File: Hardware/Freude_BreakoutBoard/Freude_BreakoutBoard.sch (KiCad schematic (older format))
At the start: 11 parts, among them J10 Conn_01x06_Female, J11 Conn_01x05_Male, J12 Conn_01x05_Female, J5 Conn_01x06_Female, J6 Conn_01x06_Male, J7 Conn_01x03_Female, J8 Conn_01x06_Male, J9 Conn_01x06_Female, U3 TLV713185PDBV

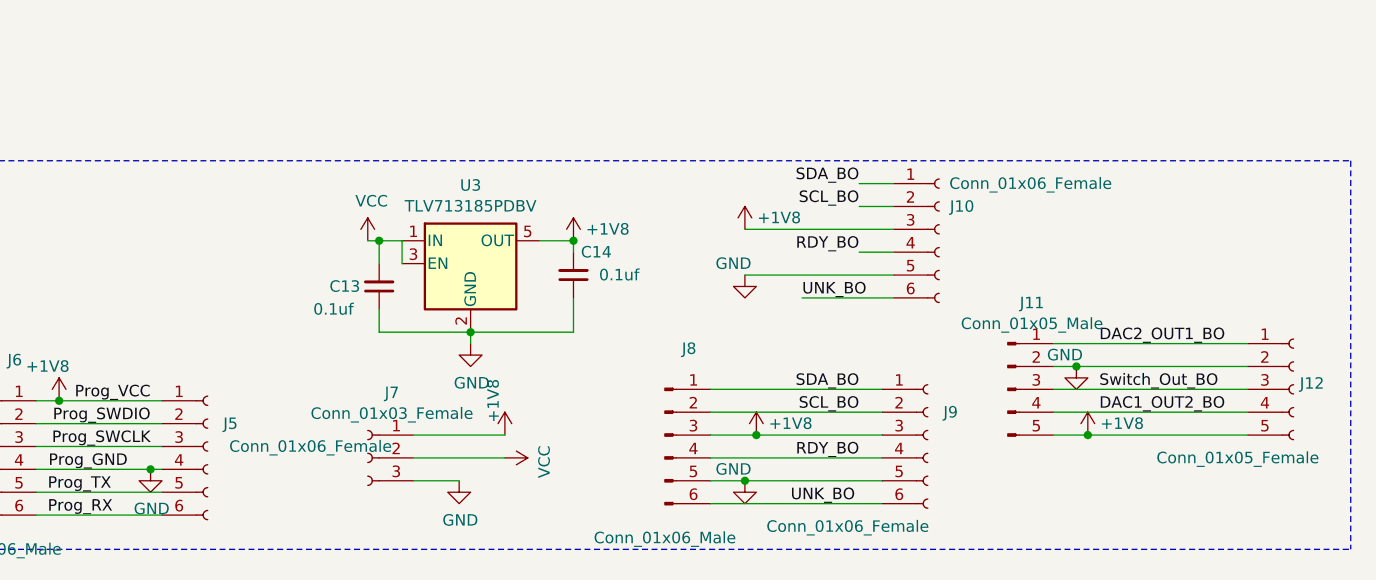
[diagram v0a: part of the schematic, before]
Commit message: resolves 10, resolves 9, resolves 6, resolves 5, add ground ring around touch sensor, add ground ring on top, separate RX from TX and include ground plane between
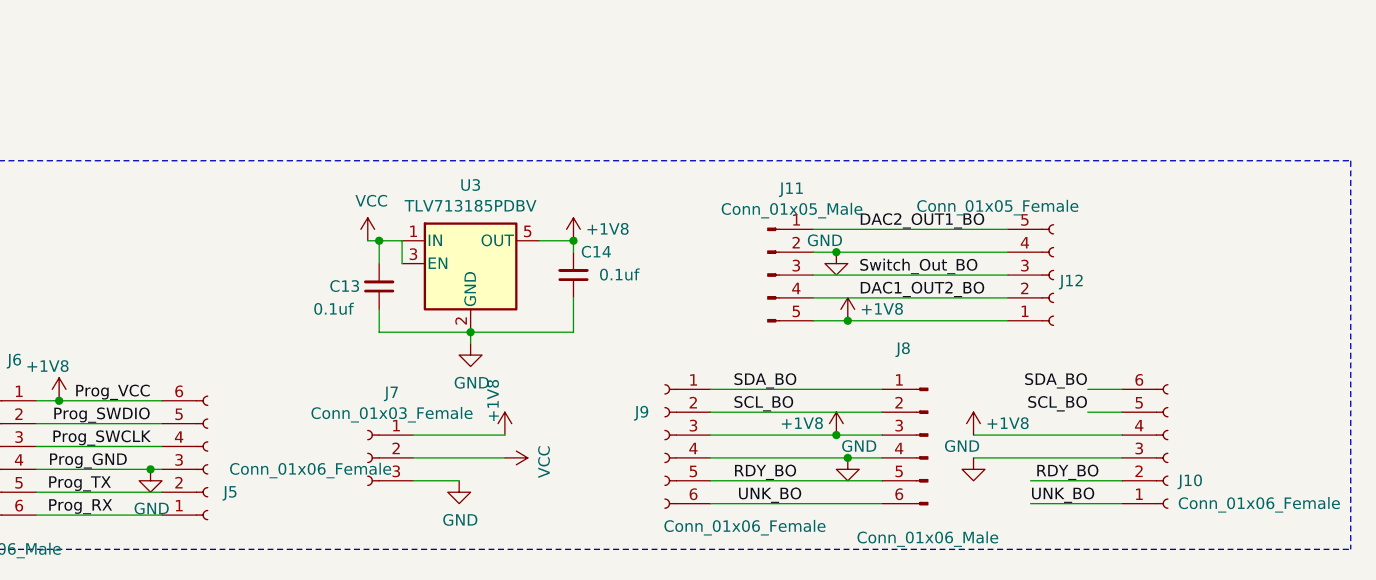
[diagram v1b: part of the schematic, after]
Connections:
- net +1V8: now also J10.4 (Pin_4), J12.1 (Pin_1), J5.6 (Pin_6); no longer J10.3 (Pin_3), J12.5 (Pin_5), J5.1 (Pin_1)
- net DAC1_OUT2_BO: now also J12.2 (Pin_2); no longer J12.4 (Pin_4)
- net DAC2_OUT1_BO: now also J12.5 (Pin_5); no longer J12.1 (Pin_1)
- net GND: now also J10.3 (Pin_3), J12.4 (Pin_4), J5.3 (Pin_3), J8.4 (Pin_4), J9.4 (Pin_4); no longer J10.5 (Pin_5), J12.2 (Pin_2), J5.4 (Pin_4), J8.5 (Pin_5), J9.5 (Pin_5)
- net Prog_RX: now also J5.1 (Pin_1); no longer J5.6 (Pin_6)
- net Prog_SWCLK: now also J5.4 (Pin_4); no longer J5.3 (Pin_3)
- net Prog_SWDIO: now also J5.5 (Pin_5); no longer J5.2 (Pin_2)
- net Prog_TX: now also J5.2 (Pin_2); no longer J5.5 (Pin_5)
- net RDY_BO: now also J10.2 (Pin_2), J8.5 (Pin_5), J9.5 (Pin_5); no longer J10.4 (Pin_4), J8.4 (Pin_4), J9.4 (Pin_4)
- net SCL_BO: now also J10.5 (Pin_5); no longer J10.2 (Pin_2)
- net SDA_BO: now also J10.6 (Pin_6); no longer J10.1 (Pin_1)
- net UNK_BO: now also J10.1 (Pin_1); no longer J10.6 (Pin_6)
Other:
- moved on the sheet: J10, J11, J12, J8, J9
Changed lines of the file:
@@
 L Connector:Conn_01x06_Female J9
 U 1 1 5F2319DF
+P 5950 4250
+F 0 "J9" H 6050 4350 50  0000 C CNN
+F 1 "Conn_01x06_Female" H 5600 3850 50  0000 C CNN
+F 2 ".pretty:503480-0600" H 5950 4250 50  0001 C CNN
+F 3 "~" H 5950 4250 50  0001 C CNN
+	1    5950 4250
+	-1   0    0    -1
+$EndComp
+Text Label 6250 4050 0    50   ~ 0
+SDA_BO
+Text Label 6250 4150 0    50   ~ 0
+SCL_BO
+Text Label 6250 4450 0    50   ~ 0
+RDY_BO
+$Comp
+L Connector:Conn_01x06_Male J8
+U 1 1 5F232158
 P 7100 4250
-F 0 "J9" H 7200 4350 50  0000 C CNN
-F 1 "Conn_01x06_Female" H 6750 3850 50  0000 C CNN
-F 2 ".pretty:503480-0600" H 7100 4250 50  0001 C CNN
+F 0 "J8" H 7206 4628 50  0000 C CNN
+F 1 "Conn_01x06_Male" H 7100 3800 50  0000 C CNN
+F 2 "SparkFun-Connectors:1X06-KIT" H 7100 4250 50  0001 C CNN
 F 3 "~" H 7100 4250 50  0001 C CNN
 	1    7100 4250
-	1    0    0    -1
-$EndComp
-Text Label 6800 4050 2    50   ~ 0
-SDA_BO
-Text Label 6800 4150 2    50   ~ 0
-SCL_BO
-Text Label 6800 4350 2    50   ~ 0
-RDY_BO
-$Comp
-L Connector:Conn_01x06_Male J8
-U 1 1 5F232158
-P 5950 4250
-F 0 "J8" H 6056 4628 50  0000 C CNN
-F 1 "Conn_01x06_Male" H 5950 3800 50  0000 C CNN
-F 2 "SparkFun-Connectors:1X06-KIT" H 5950 4250 50  0001 C CNN
-F 3 "~" H 5950 4250 50  0001 C CNN
-	1    5950 4250
-	1    0    0    -1
-$EndComp
-Wire Wire Line
-	6150 4050 6900 4050
-Wire Wire Line
-	6900 4150 6150 4150
-Wire Wire Line
-	6900 4350 6150 4350
-Wire Wire Line
-	6150 4550 6900 4550
+	-1   0    0    -1
+$EndComp
+Wire Wire Line
+	6900 4050 6150 4050
+Wire Wire Line
+	6150 4150 6900 4150
+Wire Wire Line
+	6900 4550 6150 4550
 $Comp
 L power:+1V8 #PWR0122
 U 1 1 5F274120
-P 6350 4250
-F 0 "#PWR0122" H 6350 4100 50  0001 C CNN
-F 1 "+1V8" H 6500 4300 50  0000 C CNN
-F 2 "" H 6350 4250 50  0001 C CNN
-F 3 "" H 6350 4250 50  0001 C CNN
-	1    6350 4250
-	1    0    0    -1
-$EndComp
-Wire Wire Line
-	6150 4250 6350 4250
-Connection ~ 6350 4250
-Wire Wire Line
-	6350 4250 6900 4250
+P 6700 4250
+F 0 "#PWR0122" H 6700 4100 50  0001 C CNN
+F 1 "+1V8" H 6850 4300 50  0000 C CNN
+F 2 "" H 6700 4250 50  0001 C CNN
+F 3 "" H 6700 4250 50  0001 C CNN
+	1    6700 4250
+	-1   0    0    -1
+$EndComp
+Wire Wire Line
+	6900 4250 6700 4250
+Connection ~ 6700 4250
+Wire Wire Line
+	6700 4250 6150 4250
 $Comp
 L power:+1V8 #PWR0123
@@
 L Connector:Conn_01x05_Female J12
 U 1 1 5F274440
-P 8700 4050
-F 0 "J12" H 8727 4076 50  0000 L CNN
-F 1 "Conn_01x05_Female" H 8100 3750 50  0000 L CNN
-F 2 ".pretty:503480-0500" H 8700 4050 50  0001 C CNN
-F 3 "~" H 8700 4050 50  0001 C CNN
-	1    8700 4050
-	1    0    0    -1
-$EndComp
-Text Label 7850 3850 0    50   ~ 0
+P 7650 3550
+F 0 "J12" H 7677 3576 50  0000 L CNN
+F 1 "Conn_01x05_Female" H 7050 3250 50  0000 L CNN
+F 2 ".pretty:503480-0500" H 7650 3550 50  0001 C CNN
+F 3 "~" H 7650 3550 50  0001 C CNN
+	1    7650 3550
+	1    0    0    1
+$EndComp
+Text Label 6800 3350 0    50   ~ 0
 DAC2_OUT1_BO
-Text Label 7850 4150 0    50   ~ 0
+Text Label 6800 3650 0    50   ~ 0
 DAC1_OUT2_BO
-Text Label 7850 4050 0    50   ~ 0
+Text Label 6800 3550 0    50   ~ 0
 Switch_Out_BO
 $Comp
 L Connector:Conn_01x05_Male J11
 U 1 1 5F28FAAB
-P 7450 4050
-F 0 "J11" H 7556 4428 50  0000 C CNN
-F 1 "Conn_01x05_Male" H 7556 4337 50  0000 C CNN
-F 2 "SparkFun-Connectors:1X05" H 7450 4050 50  0001 C CNN
-F 3 "~" H 7450 4050 50  0001 C CNN
-	1    7450 4050
+P 6400 3550
+F 0 "J11" H 6506 3928 50  0000 C CNN
+F 1 "Conn_01x05_Male" H 6506 3837 50  0000 C CNN
+F 2 "SparkFun-Connectors:1X05" H 6400 3550 50  0001 C CNN
+F 3 "~" H 6400 3550 50  0001 C CNN
+	1    6400 3550
 	1    0    0    -1
 $EndComp
@@
 L power:+1V8 #PWR0124
 U 1 1 5F28FB0B
-P 7800 4250
-F 0 "#PWR0124" H 7800 4100 50  0001 C CNN
-F 1 "+1V8" H 7950 4300 50  0000 C CNN
-F 2 "" H 7800 4250 50  0001 C CNN
-F 3 "" H 7800 4250 50  0001 C CNN
-	1    7800 4250
-	1    0    0    -1
-$EndComp
-Wire Wire Line
-	7650 4150 8500 4150
-Wire Wire Line
-	8500 4250 7800 4250
-Connection ~ 7800 4250
-Wire Wire Line
-	7800 4250 7650 4250
-Wire Wire Line
-	7650 4050 8500 4050
-Wire Wire Line
-	7650 3850 8500 3850
+P 6750 3750
+F 0 "#PWR0124" H 6750 3600 50  0001 C CNN
+F 1 "+1V8" H 6900 3800 50  0000 C CNN
+F 2 "" H 6750 3750 50  0001 C CNN
+F 3 "" H 6750 3750 50  0001 C CNN
+	1    6750 3750
+	1    0    0    -1
+$EndComp
+Wire Wire Line
+	6600 3650 7450 3650
+Wire Wire Line
+	7450 3750 6750 3750
+Connection ~ 6750 3750
+Wire Wire Line
+	6750 3750 6600 3750
+Wire Wire Line
+	6600 3550 7450 3550
+Wire Wire Line
+	6600 3350 7450 3350
 $Comp
 L power:VCC #PWR0128
@@
 L Connector:Conn_01x06_Female J10
 U 1 1 5F3EB865
-P 7150 3350
-F 0 "J10" H 7250 3450 50  0000 C CNN
-F 1 "Conn_01x06_Female" H 7550 3550 50  0000 C CNN
-F 2 ".pretty:503480-0600" H 7150 3350 50  0001 C CNN
-F 3 "~" H 7150 3350 50  0001 C CNN
-	1    7150 3350
-	1    0    0    -1
-$EndComp
-Text Label 6800 3150 2    50   ~ 0
+P 8150 4350
+F 0 "J10" H 8250 4450 50  0000 C CNN
+F 1 "Conn_01x06_Female" H 8550 4550 50  0000 C CNN
+F 2 ".pretty:503480-0600" H 8150 4350 50  0001 C CNN
+F 3 "~" H 8150 4350 50  0001 C CNN
+	1    8150 4350
+	1    0    0    1
+$EndComp
+Text Label 7800 4050 2    50   ~ 0
 SDA_BO
-Text Label 6800 3250 2    50   ~ 0
+Text Label 7800 4150 2    50   ~ 0
 SCL_BO
 $Comp
 L power:+1V8 #PWR0133
 U 1 1 5F3F809E
-P 6300 3350
-F 0 "#PWR0133" H 6300 3200 50  0001 C CNN
-F 1 "+1V8" H 6450 3400 50  0000 C CNN
-F 2 "" H 6300 3350 50  0001 C CNN
-F 3 "" H 6300 3350 50  0001 C CNN
-	1    6300 3350
-	1    0    0    -1
-$EndComp
-Text Label 6800 3450 2    50   ~ 0
+P 7300 4250
+F 0 "#PWR0133" H 7300 4100 50  0001 C CNN
+F 1 "+1V8" H 7450 4300 50  0000 C CNN
+F 2 "" H 7300 4250 50  0001 C CNN
+F 3 "" H 7300 4250 50  0001 C CNN
+	1    7300 4250
+	1    0    0    -1
+$EndComp
+Text Label 7850 4450 2    50   ~ 0
 RDY_BO
-Text Label 6500 4550 0    50   ~ 0
+Text Label 6550 4550 2    50   ~ 0
 UNK_BO
-Text Label 6550 3650 0    50   ~ 0
+Text Label 7550 4550 0    50   ~ 0
 UNK_BO
 Wire Wire Line
-	6950 3150 6800 3150
-Wire Wire Line
-	6950 3250 6800 3250
-Wire Wire Line
-	6950 3350 6300 3350
-Wire Wire Line
-	6950 3450 6800 3450
-Wire Wire Line
-	6950 3550 6300 3550
-Wire Wire Line
-	6950 3650 6550 3650
+	7950 4050 7800 4050
+Wire Wire Line
+	7950 4150 7800 4150
+Wire Wire Line
+	7950 4250 7300 4250
+Wire Wire Line
+	7950 4450 7550 4450
+Wire Wire Line
+	7950 4550 7550 4550
 $Comp
 L power:GND #PWR0121
@@
 L power:GND #PWR0127
 U 1 1 5F37C7FE
-P 6300 4450
-F 0 "#PWR0127" H 6300 4200 50  0001 C CNN
-F 1 "GND" H 6250 4500 50  0000 C CNN
-F 2 "" H 6300 4450 50  0001 C CNN
-F 3 "" H 6300 4450 50  0001 C CNN
-	1    6300 4450
-	1    0    0    -1
-$EndComp
-Wire Wire Line
-	6150 4450 6300 4450
-Connection ~ 6300 4450
-Wire Wire Line
-	6300 4450 6900 4450
+P 6750 4350
+F 0 "#PWR0127" H 6750 4100 50  0001 C CNN
+F 1 "GND" H 6700 4400 50  0000 C CNN
+F 2 "" H 6750 4350 50  0001 C CNN
+F 3 "" H 6750 4350 50  0001 C CNN
+	1    6750 4350
+	-1   0    0    -1
+$EndComp
 $Comp
 L power:GND #PWR0132
 U 1 1 5F37D102
-P 7750 3950
-F 0 "#PWR0132" H 7750 3700 50  0001 C CNN
-F 1 "GND" H 7700 4000 50  0000 C CNN
-F 2 "" H 7750 3950 50  0001 C CNN
-F 3 "" H 7750 3950 50  0001 C CNN
-	1    7750 3950
-	1    0    0    -1
-$EndComp
-Wire Wire Line
-	7650 3950 7750 3950
-Connection ~ 7750 3950
-Wire Wire Line
-	7750 3950 8500 3950
+P 6700 3450
+F 0 "#PWR0132" H 6700 3200 50  0001 C CNN
+F 1 "GND" H 6650 3500 50  0000 C CNN
+F 2 "" H 6700 3450 50  0001 C CNN
+F 3 "" H 6700 3450 50  0001 C CNN
+	1    6700 3450
+	1    0    0    -1
+$EndComp
+Wire Wire Line
+	6600 3450 6700 3450
+Connection ~ 6700 3450
+Wire Wire Line
+	6700 3450 7450 3450
 $Comp
 L power:GND #PWR0134
 U 1 1 5F37DC1D
-P 6300 3550
-F 0 "#PWR0134" H 6300 3300 50  0001 C CNN
-F 1 "GND" H 6250 3600 50  0000 C CNN
-F 2 "" H 6300 3550 50  0001 C CNN
-F 3 "" H 6300 3550 50  0001 C CNN
-	1    6300 3550
+P 7300 4350
+F 0 "#PWR0134" H 7300 4100 50  0001 C CNN
+F 1 "GND" H 7250 4400 50  0000 C CNN
+F 2 "" H 7300 4350 50  0001 C CNN
+F 3 "" H 7300 4350 50  0001 C CNN
+	1    7300 4350
 	1    0    0    -1
 $EndComp
@@
 L Connector:Conn_01x06_Female J5
 U 1 1 5F38A8DF
-P 3950 4300
-F 0 "J5" H 4050 4400 50  0000 C CNN
-F 1 "Conn_01x06_Female" H 4400 4300 50  0000 C CNN
-F 2 ".pretty:503480-0600" H 3950 4300 50  0001 C CNN
-F 3 "~" H 3950 4300 50  0001 C CNN
-	1    3950 4300
-	1    0    0    -1
+P 3950 4400
+F 0 "J5" H 4050 4500 50  0000 C CNN
+F 1 "Conn_01x06_Female" H 4400 4400 50  0000 C CNN
+F 2 ".pretty:503480-0600" H 3950 4400 50  0001 C CNN
+F 3 "~" H 3950 4400 50  0001 C CNN
+	1    3950 4400
+	1    0    0    1
 $EndComp
 $Comp
@@
 Text Label 3250 4600 0    50   ~ 0
 Prog_RX
+Wire Wire Line
+	6150 4450 6900 4450
+Connection ~ 6750 4350
+Wire Wire Line
+	6750 4350 6900 4350
+Wire Wire Line
+	6150 4350 6750 4350
+Wire Wire Line
+	7300 4350 7950 4350
 $EndSCHEMATC
